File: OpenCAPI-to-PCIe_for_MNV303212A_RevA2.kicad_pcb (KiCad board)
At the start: 4 copper layers, 51.3 x 40.6 mm, 10 parts, among them J1 OpenCAPI_AAC_Host, J2 Conn_01x06, J3 Bus_PCI_Express_x8

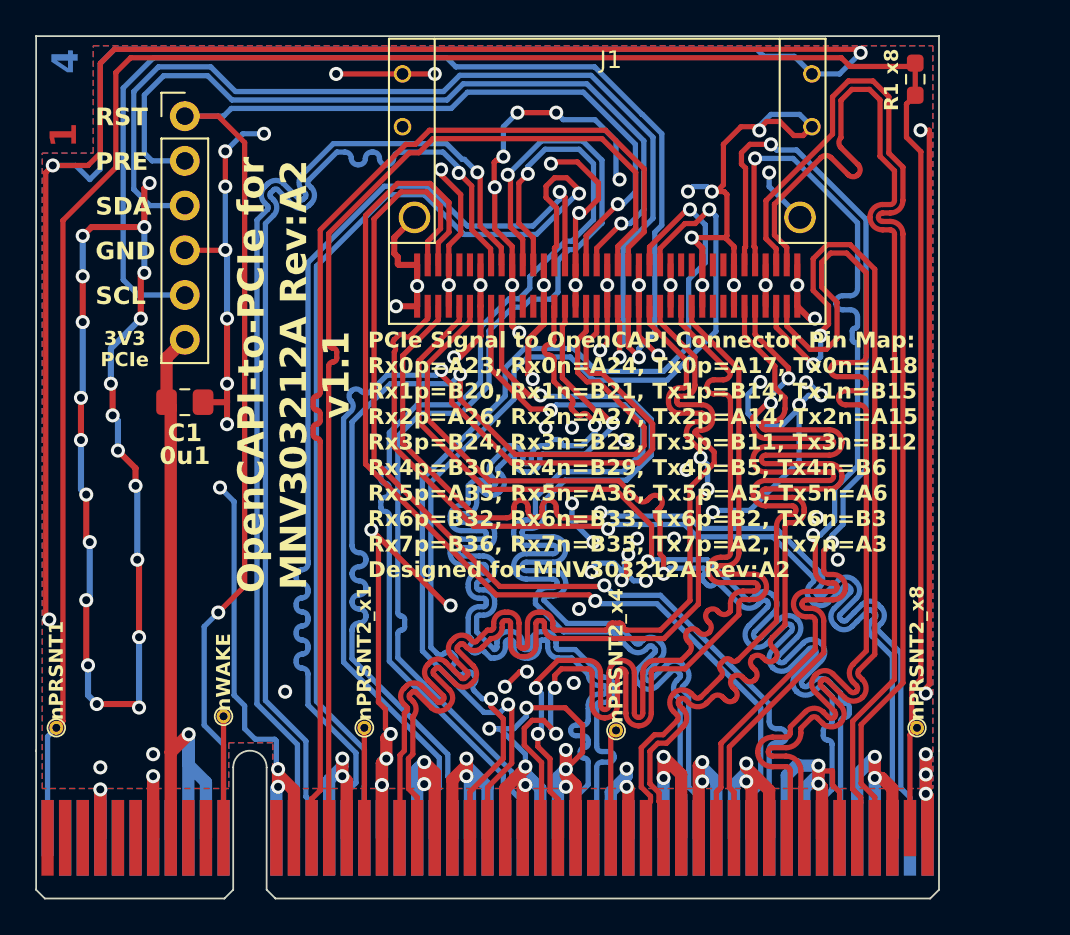
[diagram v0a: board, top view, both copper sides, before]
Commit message: Fixed GND Plane
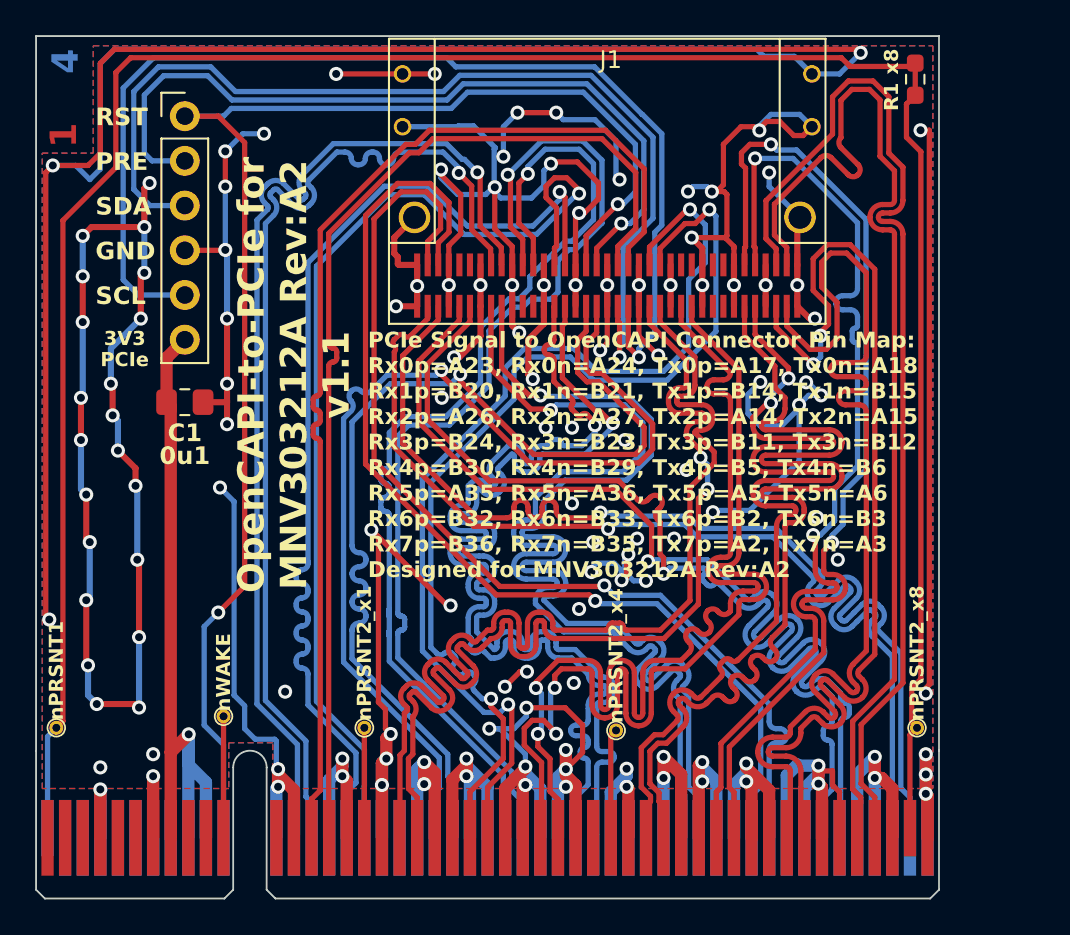
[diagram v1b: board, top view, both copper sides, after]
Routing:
- net GND: track 671.5 -> 930.6 mm, vias 132 -> 133
- net Rx1_N: track 59.3 -> 58.6 mm
- net Rx1_P: track 59.3 -> 58.7 mm
